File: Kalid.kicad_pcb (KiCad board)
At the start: 4 copper layers, 90 x 40 mm, 132 parts, among them J1 USB_A, J2 USB-C Receptacle, J3 USB_A, J31 DC Connector, J4 USB_A, J5 USB_A, U1 TPS62933, U2 TPS62933, U3 GL3523-OTY30, U4 USB-PD, U5 LPW5209AB5F, U6 LPW5209AB5F, U7 LPW5209AB5F, U8 LPW5209AB5F, U9 W25Q128JVS, Y1 Crystal 25MHz 2016

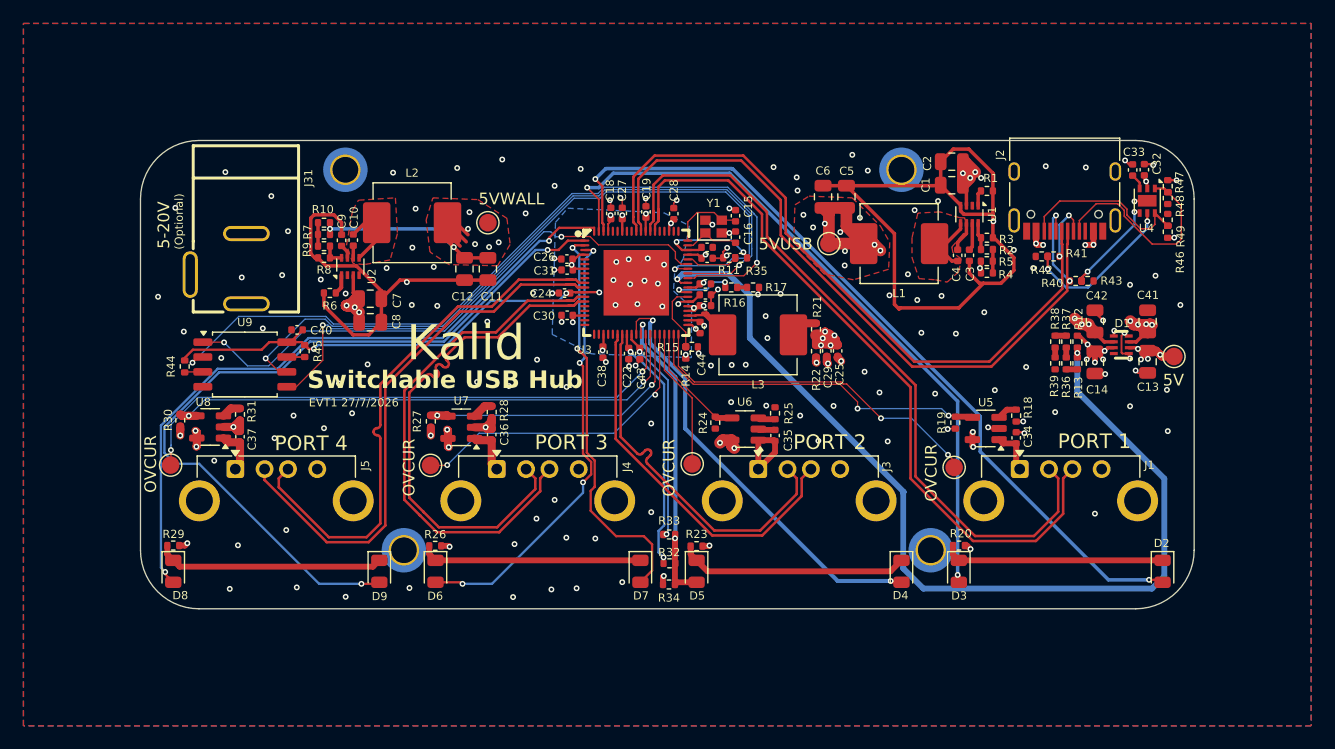
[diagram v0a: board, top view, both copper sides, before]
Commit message: fix 90-ohm trace width
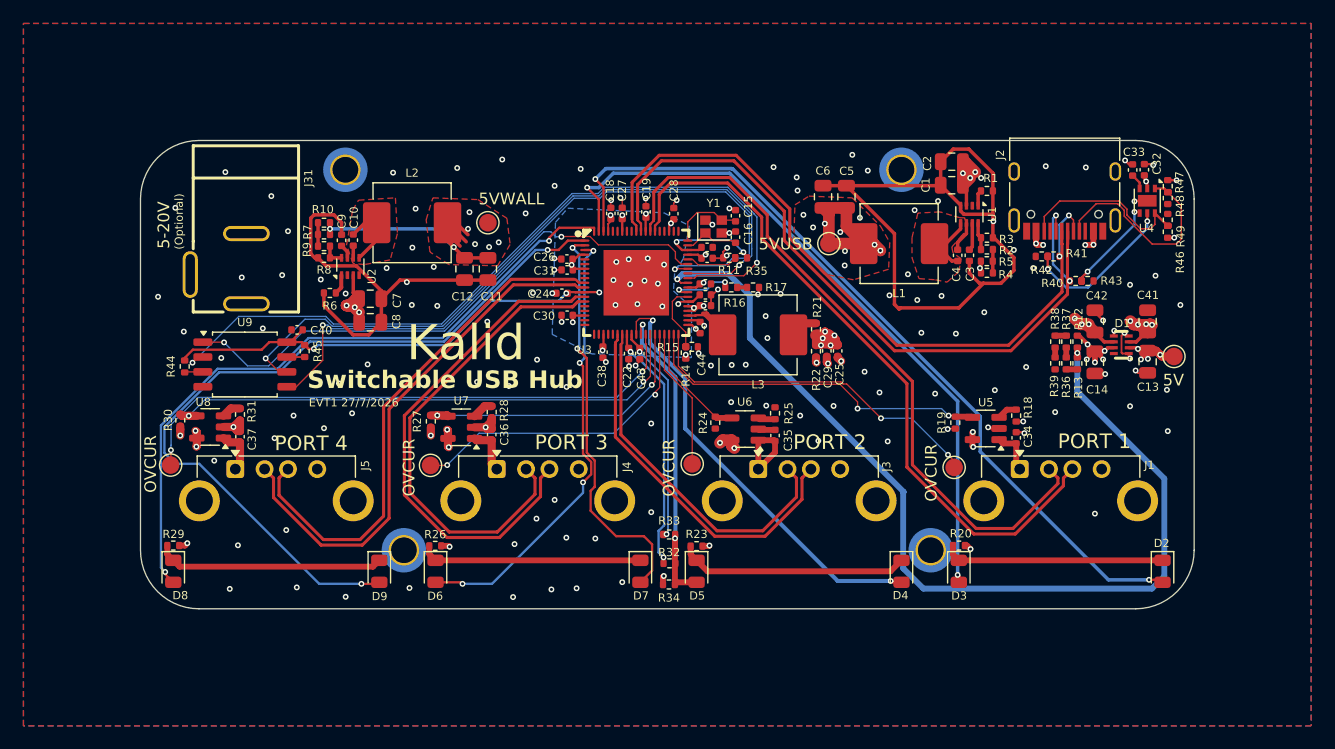
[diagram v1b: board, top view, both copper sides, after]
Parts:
- moved C24 0.22 mm to (136.0, 78.0)
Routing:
- net /Hierarchy/USB/P1_D+: track 63.4 -> 59.3 mm
- net /Hierarchy/USB/P1_D-: track 63.2 -> 59.3 mm
- net /Hierarchy/USB/P3_D-: track 45.3 -> 42.8 mm
- net /Hierarchy/USB/P4_D+: track 47.4 -> 44.9 mm
- net /Hierarchy/USB/P4_D-: track 47.8 -> 46.1 mm
- net /Hierarchy/USB/P3_D+: track 45.7 -> 44.2 mm
- net /Hierarchy/USB/USB_UFP_D+: track 66.3 -> 64.9 mm
- net /Hierarchy/USB/USB_UFP_D-: track 64.0 -> 62.6 mm
- net /Hierarchy/USB/P2_D-: track 32.3 -> 30.9 mm
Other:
- board text added: "Manufacture using JLC04161H-7628 (Standard/Finished thickness1.59mm±10%) 0.2037"

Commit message: develop evt2
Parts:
- removed C17: Cap 4.7uF 0402, Capacitor_SMD:C_0402_1005Metric
- removed R44, R45: R 0 ohm 0402, Resistor_SMD:R_0402_1005Metric
- added R50: R 10k 0402, Resistor_SMD:R_0402_1005Metric, F.Cu at (161.1, 67.2)
- added R51: R 10k 0402, Resistor_SMD:R_0402_1005Metric, F.Cu at (159.2, 67.2)
- added R52: R 10k 0402, Resistor_SMD:R_0402_1005Metric, F.Cu at (162.1, 67.2)
- added R53: R 10k 0402, Resistor_SMD:R_0402_1005Metric, F.Cu at (158.3, 67.2)
- added R54: R 10k 0402, Resistor_SMD:R_0402_1005Metric, F.Cu at (129.2, 69.0)
- added R55: R 10k 0402, Resistor_SMD:R_0402_1005Metric, F.Cu at (129.2, 67.1)
- added R56: R 10k 0402, Resistor_SMD:R_0402_1005Metric, F.Cu at (130.1, 69.0)
- added R57: R 10k 0402, Resistor_SMD:R_0402_1005Metric, F.Cu at (130.1, 67.1)
- added TP7: TestPoint, TestPoint:TestPoint_Pad_D1.5mm, F.Cu at (182.6, 75.4)
- L3: value 10uH, 4.5A -> L 2.2uH 2A; footprint Inductor_SMD:L_Changjiang_FXL0630 -> Kalid:IND-SMD_L3.0-W3.0_LQH3NPN
- R14, R15: value R 10k 0402 -> R 0 ohm 0402
- R36: value R 10k 0402 -> R 5.1k 0402
- moved R37 75.8 mm to (103.3, 84.7), turned to 180 degrees
- moved R38 63.6 mm to (114.5, 83.5), turned to 0 degrees
- moved R13 35.6 mm to (147.3, 70.1), turned to 180 degrees
- moved R36 33.0 mm to (149.2, 70.1), turned to 0 degrees
- moved R39 27.4 mm to (151.4, 78.2), turned to 180 degrees
- moved R12 27.1 mm to (153.2, 78.2), turned to 0 degrees
- moved R4 17.7 mm to (156.9, 67.6)
- moved R5 17.7 mm to (156.9, 66.7)
- moved R8 14.4 mm to (128.3, 67.1), turned to -90 degrees
- moved R9 14.1 mm to (127.3, 67.1), turned to 90 degrees
- moved R2 14.1 mm to (160.2, 67.2), turned to 90 degrees
- moved R7 13.2 mm to (128.3, 68.9), turned to -90 degrees
- moved R10 12.0 mm to (127.3, 68.9), turned to -90 degrees
- moved R3 10.4 mm to (162.8, 69.0), turned to 90 degrees
- moved C25 3.12 mm to (156.4, 82.9)
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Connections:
- net Net-(U3B-P_SPI_CK) renamed /Hierarchy/USB/SPI_CLK
- net Net-(U3B-P_SPI_CZ) renamed /Hierarchy/USB/SPI_CS
- R13 pad 1: Net-(U3B-RESETJ) -> Net-(U3A-VBUS)
- R13 pad 2: Net-(R13-Pad2) -> GND
- R15 pad 2: GND -> +V5V
- R2 pad 1: Net-(U1-FB) -> Net-(R2-Pad1)
- R36 pad 1: Net-(R13-Pad2) -> Net-(U3A-VBUS)
- R36 pad 2: Net-(R36-Pad2) -> +V5VUSB
- R37 pad 1: Net-(R36-Pad2) -> Net-(U9-~{WP}/IO_{2})
- R37 pad 2: Net-(R37-Pad2) -> +3.3V
- R38 pad 1: Net-(R38-Pad1) -> Net-(U9-~{HOLD}/~{RESET}/IO_{3})
- R38 pad 2: Net-(R37-Pad2) -> +3.3V
- R39 pad 1: GND -> Net-(U3B-RESETJ)
- R39 pad 2: Net-(R38-Pad1) -> +3.3V
- R4 pad 1: Net-(R2-Pad2) -> Net-(R4-Pad1)
- R5 pad 1: Net-(R2-Pad2) -> Net-(R4-Pad1)
- R8 pad 2: Net-(R10-Pad1) -> Net-(R55-Pad1)
- U3 pad 49: Net-(U3B-P_SPI_DO) -> /Hierarchy/USB/SPI_COPI
- U3 pad 51: Net-(U3B-P_SPI_DI) -> /Hierarchy/USB/SPI_CIPO
- U3 pad 54: +V5V -> Net-(U3A-VBUS)
- U9 pad 2: Net-(U3B-P_SPI_DO) -> /Hierarchy/USB/SPI_CIPO
- U9 pad 5: Net-(U3B-P_SPI_DI) -> /Hierarchy/USB/SPI_COPI
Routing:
- net Net-(U3B-RESETJ): track 83.4 -> 14.9 mm
- net Net-(U3B-P_SPI_DO): track 67.1 -> 0.00 mm, vias 2 -> 0
- net /Hierarchy/USB/SPI_CIPO: track 0.00 -> 64.9 mm, vias 0 -> 2
- net /Hierarchy/USB/SPI_COPI: track 0.00 -> 64.6 mm, vias 0 -> 2
- net Net-(U3B-P_SPI_DI): track 60.6 -> 0.00 mm, vias 2 -> 0
- net Net-(D6-A): track 38.5 -> 83.4 mm
- net Net-(D7-A): track 34.7 -> 69.4 mm, vias 2 -> 4
- net Net-(U2-FB): track 1.99 -> 17.4 mm, vias 0 -> 2
- net +V5VUSB: track 42.4 -> 56.0 mm
- net Net-(U1-FB): track 2.36 -> 14.7 mm, vias 0 -> 2
- net +V5V: track 35.6 -> 24.5 mm, vias 21 -> 22
- net +V5VWALL: track 97.6 -> 88.0 mm, vias 11 -> 10
- net Net-(U3A-VBUS): track 0.00 -> 6.70 mm
- net GND: track 136.4 -> 142.0 mm, vias 156 -> 143
- net +3.3V: track 77.1 -> 81.6 mm, vias 11 -> 13
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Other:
- board text added: "0"
- board text added: "0 mm"
- board text added: "0.01 mm"
- board text added: "0.0152 mm"
- board text added: "0.02"
- board text added: "0.035 mm"
- board text added: "0.1000 mm / 0.1000 mm"
- board text added: "0.2000 mm"
- board text added: "0.2104 mm"
- board text added: "1"
- board text added: "1.065 mm"
- board text added: "1.6062 mm"
- board text added: "2"
- board text added: "3"
- board text added: "3.3"
- board text added: "4"
- board text added: "4.5"
- board text added: "90.0000 mm x 40.0000 mm"
- board text added: "B.Cu"
- board text added: "B.Mask"
- board text added: "B.Paste"
- board text added: "B.Silkscreen"
- board text added: "BOARD CHARACTERISTICS"
- board text added: "Board Thickness:"
- board text added: "Board overall dimensions:"
- board text added: "Bottom Silk Screen"
- board text added: "Bottom Solder Mask"
- board text added: "Bottom Solder Paste"
- board text added: "Castellated pads:"
- board text added: "Color"
- board text added: "Copper Finish:"
- board text added: "Copper Layer Count:"
- board text added: "Dielectric"
- board text added: "ENIG"
- board text added: "EVT2 18/8/2026"
- board text added: "Edge card connectors:"
- board text added: "Epsilon R"
- board text added: "F.Cu"
- board text added: "F.Mask"
- board text added: "F.Paste"
- board text added: "F.Silkscreen"
- board text added: "FR4"
- board text added: "GND"
- board text added: "Green"
- board text added: "Impedance Control:"
- board text added: "Layer Name"
- board text added: "Loss Tangent"
- board text added: "Manufacture with JLC04161H-7628(Standard/Finished thickness1.59mm±10%) 90 ohm impedance has trace spacing of 0.12mm and impedance trace-to-copper of 0.2mm"
- board text added: "Material"
- board text added: "Min hole diameter:"
- board text added: "Min track/spacing:"
- board text added: "No"
- board text added: "Not specified"
- board text added: "PWR"
- board text added: "Plated Board Edge:"
- board text added: "Thickness (mm)"
- board text added: "Top Silk Screen"
- board text added: "Top Solder Mask"
- board text added: "Top Solder Paste"
- board text added: "Type"
- board text added: "VUSB"
- board text added: "White"
- board text added: "Yes"
- board text added: "copper"
- board text added: "core"
- board text added: "prepreg"
- board text removed: "EVT1 27/7/2026"
- board text removed: "Manufacture using JLC04161H-7628 (Standard/Finished thickness1.59mm±10%) 0.2037"
- board text removed: "PORT 1"
- board text removed: "PORT 2"
- board text removed: "PORT 3"
- board text removed: "PORT 4"

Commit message: evt3
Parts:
- removed C44: Cap 4.7uF 0402, Capacitor_SMD:C_0402_1005Metric
- added C17: Cap 12pF 0402, Capacitor_SMD:C_0402_1005Metric, F.Cu at (155.5, 81.1)
- added FB1: 120 ohm, Inductor_SMD:L_0402_1005Metric, F.Cu at (136.9, 71.1)
- added J6: Conn_01x04, Connector_PinSocket_2.54mm:PinSocket_1x04_P2.54mm_Vertical, F.Cu at (138.9, 89.5)
- added R44: R 10k 0402, Resistor_SMD:R_0402_1005Metric, F.Cu at (168.7, 89.2)
- added R45: R 10k 0402, Resistor_SMD:R_0402_1005Metric, F.Cu at (169.2, 90.6)
- added R58: R 10k 0402, Resistor_SMD:R_0402_1005Metric, F.Cu at (148.2, 89.1)
- added R59: R 10k 0402, Resistor_SMD:R_0402_1005Metric, F.Cu at (148.7, 90.5)
- added R60: R 10k 0402, Resistor_SMD:R_0402_1005Metric, F.Cu at (123.9, 89.2)
- added R61: R 10k 0402, Resistor_SMD:R_0402_1005Metric, F.Cu at (124.4, 90.6)
- added R62: R 10k 0402, Resistor_SMD:R_0402_1005Metric, F.Cu at (102.5, 89.1)
- added R63: R 10k 0402, Resistor_SMD:R_0402_1005Metric, F.Cu at (103.0, 90.5)
- added R64: R 0 ohm 0402, Resistor_SMD:R_0402_1005Metric, F.Cu at (152.9, 78.0)
- added TP11: TestPoint, TestPoint:TestPoint_Pad_D1.5mm, F.Cu at (136.6, 68.0)
- added TP8: TestPoint, TestPoint:TestPoint_Pad_D1.5mm, F.Cu at (101.8, 82.7)
- added TP9: TestPoint, TestPoint:TestPoint_Pad_D1.5mm, F.Cu at (134.1, 70.8)
- moved C36 4.21 mm to (126.8, 87.3), turned to 180 degrees
- moved C29 3.81 mm to (154.6, 79.2), turned to 90 degrees
- moved C25 3.80 mm to (155.5, 79.2), turned to 90 degrees
- moved R17 2.18 mm to (151.0, 79.0), turned to 0 degrees
- moved R28 1.57 mm to (128.8, 87.2), turned to 0 degrees
- moved R39 1.47 mm to (150.4, 77.0)
- moved R12 1.47 mm to (152.3, 77.0)
- moved R35 1.31 mm to (149.2, 75.1), turned to 180 degrees
- moved R16 0.93 mm to (151.0, 78.0)
- moved R11 0.73 mm to (150.2, 75.1), turned to 0 degrees
- moved R38 0.67 mm to (114.1, 83.0), turned to 90 degrees
- moved C21 0.40 mm to (148.6, 77.0)
- moved TP6 0.28 mm to (102.6, 93.0)
- moved TP5 0.27 mm to (124.8, 93.0)
- moved C23 0.19 mm to (148.4, 78.2)
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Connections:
- net Net-(U3B-RESETJ) renamed /Hierarchy/USB/RESETJ
- net Net-(U3F-OVCUR3J/SMC) renamed /Hierarchy/USB/SMC
- net Net-(U3G-OVCUR4J/SMD) renamed /Hierarchy/USB/SMD
- C27 pad 1: +1.2V -> +1.2VP
- C28 pad 1: +1.2V -> +1.2VP
- C30 pad 1: +1.2V -> +1.2VP
- C31 pad 1: +1.2V -> +1.2VP
- C38 pad 1: +1.2V -> +1.2VP
- L3 pad 1: Net-(L3-Pad1) -> +1.2V
- R21 pad 1: Net-(L3-Pad1) -> +1.2V
- R21 pad 2: +1.2V -> Net-(U3A-FB)
- R22 pad 1: +1.2V -> Net-(U3A-FB)
- U3 pad 17: +1.2V -> +1.2VP
- U3 pad 22: +1.2V -> +1.2VP
- U3 pad 39: +1.2V -> Net-(U3A-FB)
- U3 pad 49: /Hierarchy/USB/SPI_COPI -> /Hierarchy/USB/SPI_CIPO
- U3 pad 51: /Hierarchy/USB/SPI_CIPO -> /Hierarchy/USB/SPI_COPI
- U3 pad 60: +1.2V -> +1.2VP
- U3 pad 7: +1.2V -> +1.2VP
- U3 pad 70: +1.2V -> +1.2VP
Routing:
- net +3.3V: track 81.6 -> 136.0 mm, vias 13 -> 12
- net +1.2V: track 43.6 -> 76.6 mm, vias 14 -> 7
- net /Hierarchy/USB/RESETJ: track 14.9 -> 36.5 mm, vias 2 -> 3
- net +1.2VP: track 0.00 -> 16.0 mm, vias 0 -> 7
- net Net-(U3A-FB): track 0.00 -> 12.5 mm
- net /Hierarchy/USB/SMC: track 27.0 -> 34.8 mm
- net /Hierarchy/USB/SMD: track 48.9 -> 56.0 mm, vias 2 -> 3
- net /Hierarchy/USB/SPI_COPI: track 64.6 -> 58.9 mm
- net +V5V: track 24.5 -> 28.5 mm
- net GND: track 142.0 -> 145.5 mm, vias 143 -> 175
- net Net-(J4-VBUS): track 4.17 -> 7.36 mm
- net Net-(U3E-OVCUR2J): track 12.1 -> 14.7 mm
- net Net-(L3-Pad1): track 2.33 -> 0.00 mm
- net Net-(U3D-OVCUR1J): track 29.6 -> 31.9 mm
- net /Hierarchy/USB/SPI_CLK: track 60.0 -> 58.0 mm
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- added copper zone on In2.Cu, net +1.2VP
- removed copper zone on In2.Cu, net +1.2V
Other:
- board text added: "1.2V"
- board text added: "1.2VP"
- board text added: "3.3V"
- board text added: "EVT3 29/8/2026"
- board text added: "RST"
- board text added: "SCL"
- board text added: "SDA"
- board text removed: "EVT2 18/8/2026"

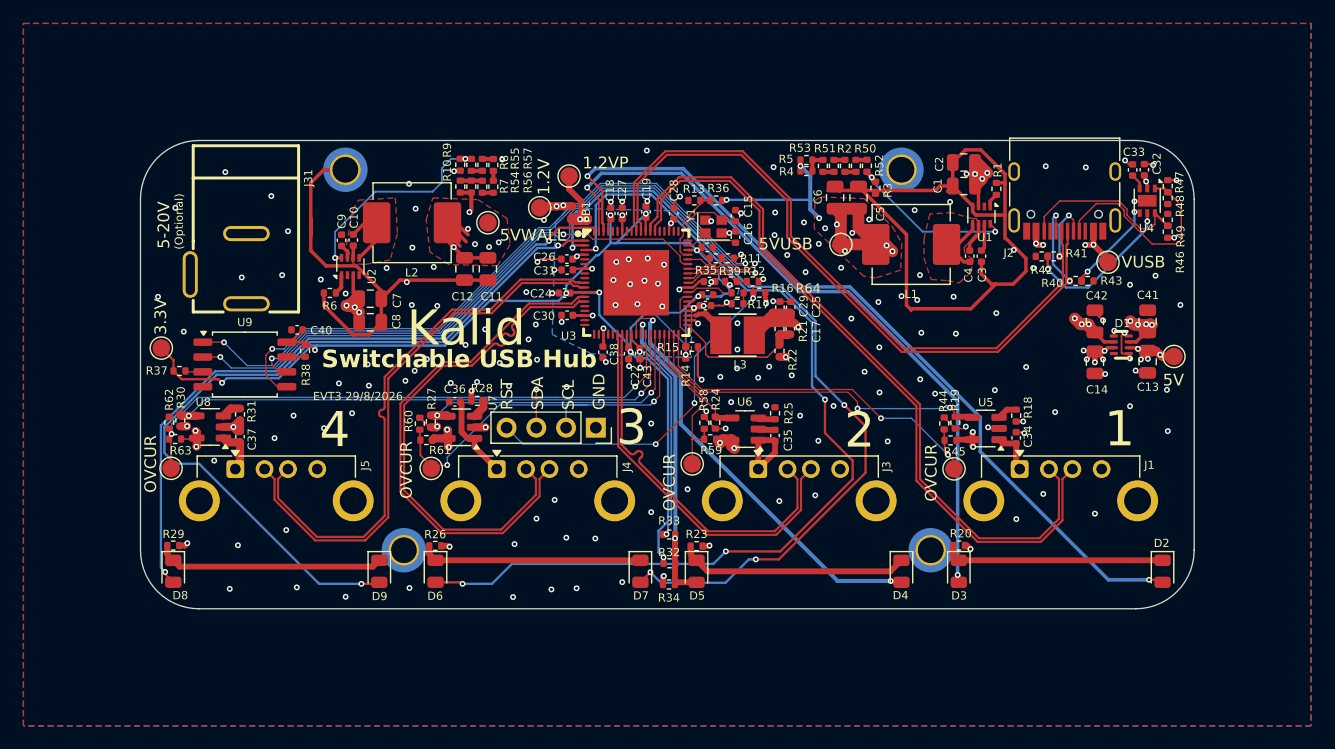
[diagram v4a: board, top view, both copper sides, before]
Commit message: evt4 - route usb3 lines
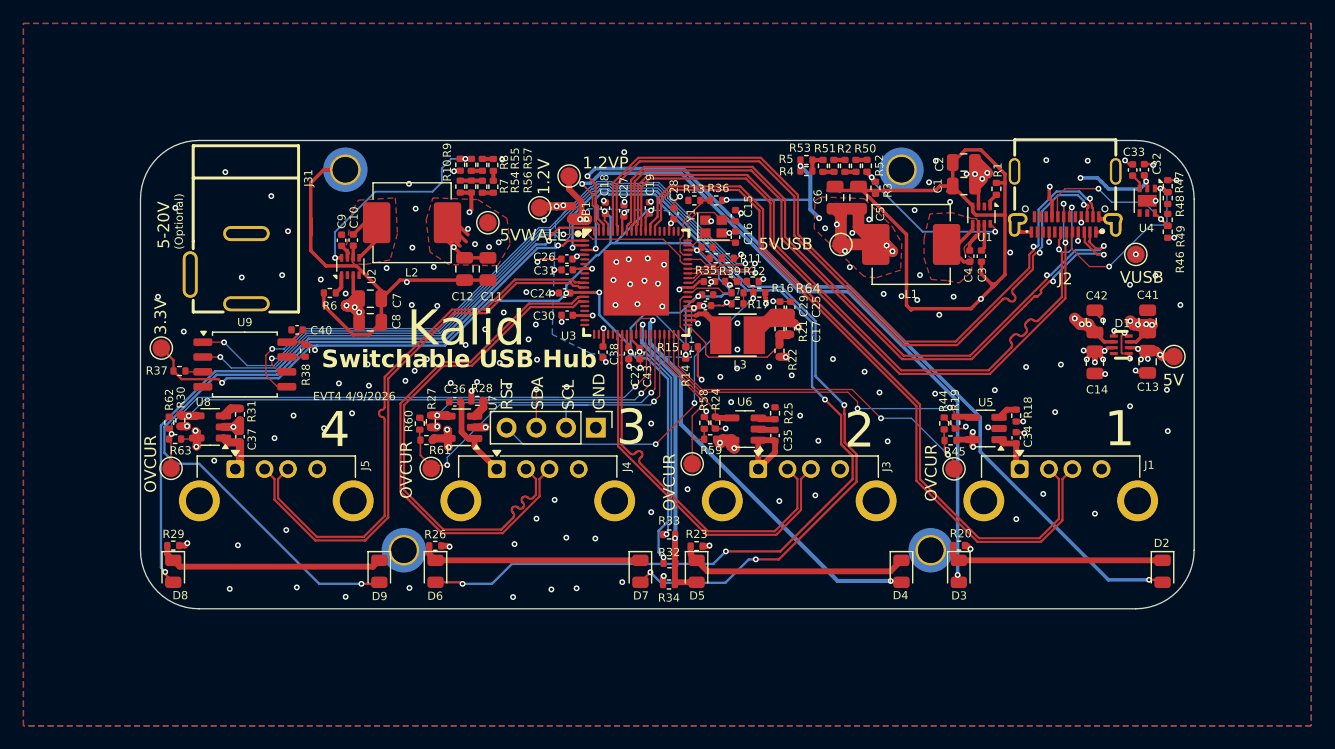
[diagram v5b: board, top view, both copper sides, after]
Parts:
- removed R40, R41, R42, R43: R 0 ohm 0402, Resistor_SMD:R_0402_1005Metric
- J2: value USB-C Receptacle -> USB_C_Receptacle; footprint Kalid:USB_C_Receptacle_HRO_TYPE-C-31-M-12 -> Kalid:USB-C-SMD_TYPE-C-24P-QT
- J6: footprint Connector_PinSocket_2.54mm:PinSocket_1x04_P2.54mm_Vertical -> Connector_PinHeader_2.54mm:PinHeader_1x04_P2.54mm_Vertical
- moved TP7 2.47 mm to (185.0, 74.7)
- moved J2 1.53 mm to (179.0, 70.2)
- moved C18 0.65 mm to (139.7, 70.8)
- moved C19 0.46 mm to (143.5, 70.8)
- moved C27 0.26 mm to (141.3, 71.0)
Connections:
- U3 pad 68: unconnected-(U3C-TXN1_P0-Pad68) -> /Hierarchy/USB/USB_UFP_TX-
- U3 pad 69: unconnected-(U3C-TXP1_P0-Pad69) -> /Hierarchy/USB/USB_UFP_TX+
- U3 pad 71: unconnected-(U3C-RXN1_P0-Pad71) -> /Hierarchy/USB/USB_UFP_RX-
- U3 pad 72: unconnected-(U3C-RXP1_P0-Pad72) -> /Hierarchy/USB/USB_UFP_RX+
- U4 pad 4: Net-(U4-D+) -> unconnected-(U4-D+-Pad4)
- U4 pad 5: Net-(U4-D-) -> unconnected-(U4-D--Pad5)
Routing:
- net /Hierarchy/USB/USB_UFP_RX+: track 0.00 -> 64.1 mm, vias 0 -> 2
- net /Hierarchy/USB/USB_UFP_RX-: track 0.00 -> 64.1 mm, vias 0 -> 2
- net /Hierarchy/USB/USB_UFP_TX+: track 0.00 -> 60.5 mm, vias 0 -> 2
- net /Hierarchy/USB/USB_UFP_TX-: track 0.00 -> 60.5 mm, vias 0 -> 2
- net Net-(U4-D-): track 13.6 -> 0.00 mm, vias 2 -> 0
- net +VUSBIN: track 40.9 -> 49.4 mm, vias 9 -> 11
- net Net-(U4-D+): track 8.25 -> 0.00 mm, vias 2 -> 0
- net /Hierarchy/USB/USB_UFP_D+: track 65.2 -> 62.2 mm
- net +3.3V: track 136.0 -> 138.1 mm
- net /Hierarchy/USB/USB_UFP_D-: track 62.9 -> 64.9 mm
- net /Hierarchy/USB/CC1: track 17.8 -> 16.0 mm, vias 0 -> 2
- net /Hierarchy/USB/CC2: track 15.2 -> 13.5 mm, vias 0 -> 2
- net Net-(D3-A): track 59.9 -> 60.7 mm
- net Net-(D6-A): track 82.3 -> 82.9 mm
- net /Hierarchy/USB/P1_D-: track 61.8 -> 61.2 mm
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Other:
- board text added: "EVT4 4/9/2026"
- board text removed: "EVT3 29/8/2026"
